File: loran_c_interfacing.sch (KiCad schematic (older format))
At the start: 16 parts, among them P401 SPI Bus A, P402 SPI Bus B, U401 74AC14, U402 74AC14

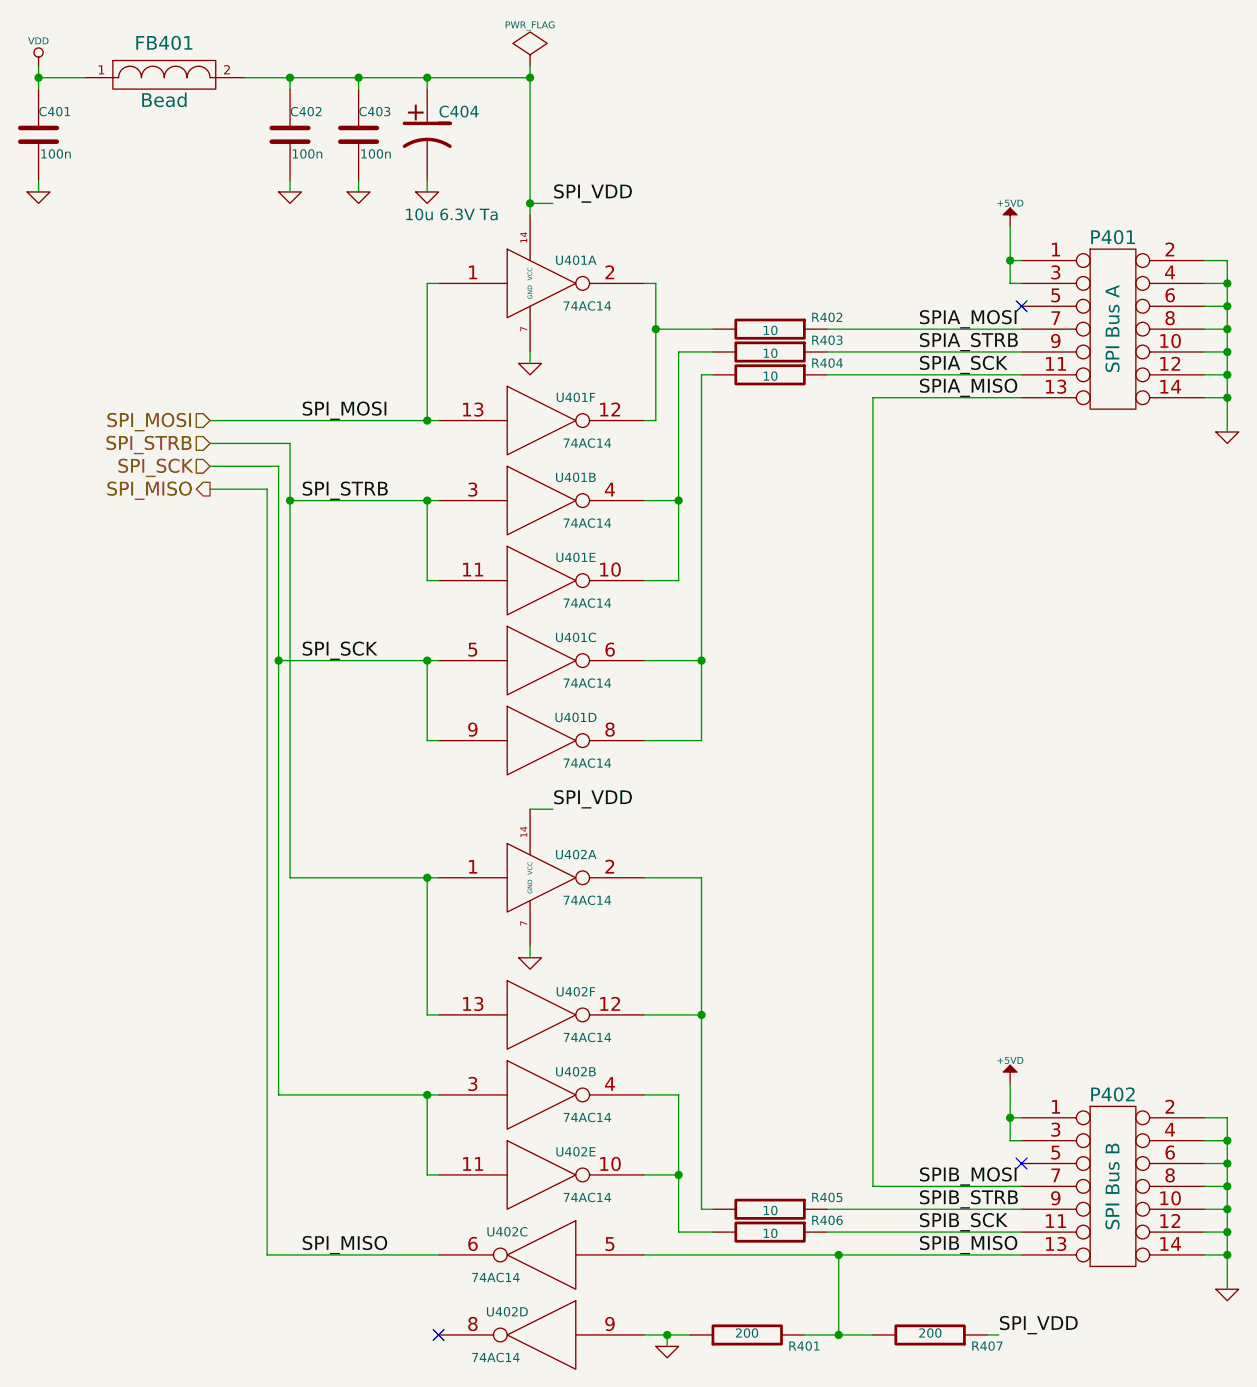
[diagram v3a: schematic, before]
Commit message: Update: minor schematic rework (due to PCB routing), PCB routing in early stage
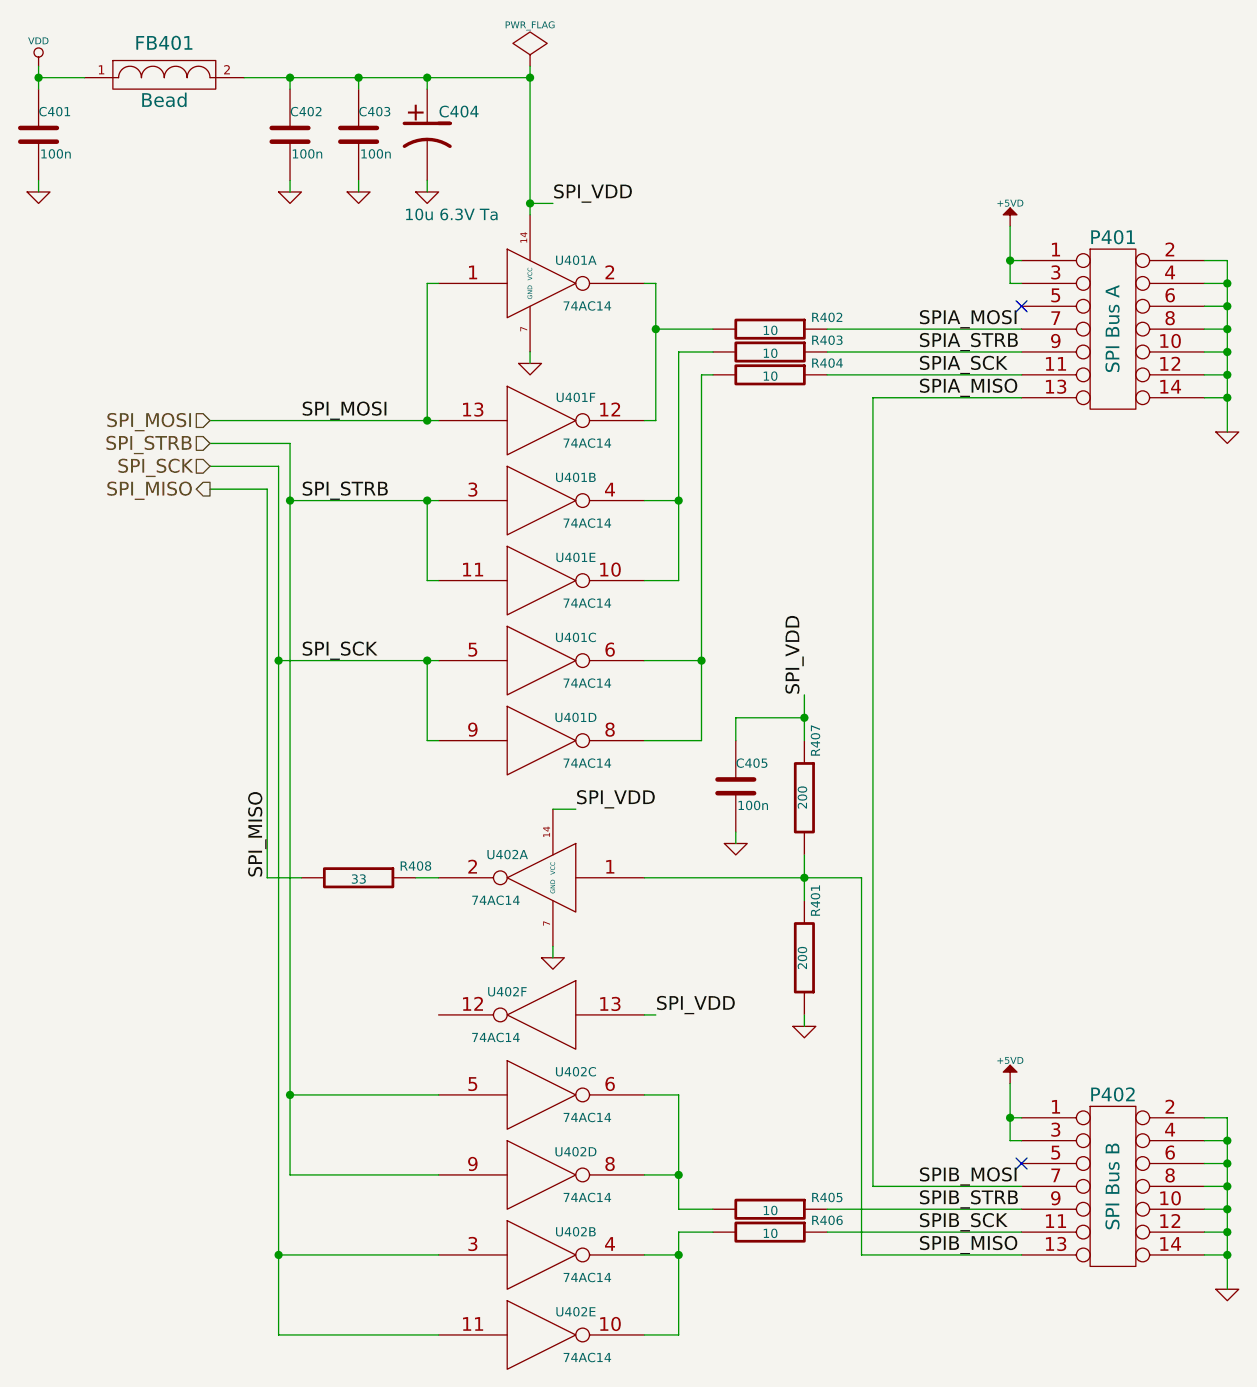
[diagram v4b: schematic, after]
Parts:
- added C405: 100n, w_smd_capacitors:c_1206, symbol C
- added R408: 33, w_smd_resistors:r_1206, symbol R
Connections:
- net GND: now also C405.2; no longer U402.9
- net SPIB_MISO: now also U402.1; no longer U402.5
- net SPI_MISO: now also R408.2; no longer U402.6
- net SPI_SCK: now also U402.11, U402.3; no longer U402.11, U402.3
- net SPI_STRB: now also U402.5, U402.9; no longer U402.1, U402.13
- net SPI_VDD: now also U402.13, C405.1
- new net: R408.1, U402.2
- new net: R405.2, U402.6, U402.8
- new net: R406.2, U402.10, U402.4
- now unconnected: U402.12
- no-connect marks 3 -> 2
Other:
- moved on the sheet: R401, R407
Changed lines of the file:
@@
 $EndComp
 $Comp
-L GND #PWR058
+L GND #PWR078
 U 1 1 52DAD917
 P 8600 2350
-F 0 "#PWR058" H 8600 2350 30  0001 C CNN
+F 0 "#PWR078" H 8600 2350 30  0001 C CNN
 F 1 "GND" H 8600 2280 30  0001 C CNN
 F 2 "" H 8600 2350 60  0000 C CNN
@@
 $EndComp
 $Comp
-L +5VD #PWR059
+L +5VD #PWR079
 U 1 1 52DAE845
 P 7650 1450
-F 0 "#PWR059" H 7650 1400 20  0001 C CNN
+F 0 "#PWR079" H 7650 1400 20  0001 C CNN
 F 1 "+5VD" H 7650 1550 30  0000 C CNN
 F 2 "" H 7650 1450 60  0000 C CNN
@@
 $EndComp
 $Comp
-L GND #PWR060
+L GND #PWR080
 U 1 1 52DAF90C
 P 8600 6100
-F 0 "#PWR060" H 8600 6100 30  0001 C CNN
+F 0 "#PWR080" H 8600 6100 30  0001 C CNN
 F 1 "GND" H 8600 6030 30  0001 C CNN
 F 2 "" H 8600 6100 60  0000 C CNN
@@
 $EndComp
 $Comp
-L +5VD #PWR061
+L +5VD #PWR081
 U 1 1 52DAF91B
 P 7650 5200
-F 0 "#PWR061" H 7650 5150 20  0001 C CNN
+F 0 "#PWR081" H 7650 5150 20  0001 C CNN
 F 1 "+5VD" H 7650 5300 30  0000 C CNN
 F 2 "" H 7650 5200 60  0000 C CNN
@@
 $EndComp
 $Comp
-L GND #PWR062
+L GND #PWR082
 U 1 1 52DD7CC9
 P 5550 2050
-F 0 "#PWR062" H 5550 2050 30  0001 C CNN
+F 0 "#PWR082" H 5550 2050 30  0001 C CNN
 F 1 "GND" H 5550 1980 30  0001 C CNN
 F 2 "" H 5550 2050 60  0000 C CNN
@@
 F 3 "" H 5600 4300 60  0000 C CNN
 	1    5600 4300
-	1    0    0    -1
-$EndComp
-$Comp
-L GND #PWR063
+	-1   0    0    -1
+$EndComp
+$Comp
+L GND #PWR083
 U 1 1 52DD892D
-P 5550 4650
-F 0 "#PWR063" H 5550 4650 30  0001 C CNN
-F 1 "GND" H 5550 4580 30  0001 C CNN
-F 2 "" H 5550 4650 60  0000 C CNN
-F 3 "" H 5550 4650 60  0000 C CNN
-	1    5550 4650
-	1    0    0    -1
-$EndComp
-Text Label 5650 4000 0    60   ~ 0
+P 5650 4650
+F 0 "#PWR083" H 5650 4650 30  0001 C CNN
+F 1 "GND" H 5650 4580 30  0001 C CNN
+F 2 "" H 5650 4650 60  0000 C CNN
+F 3 "" H 5650 4650 60  0000 C CNN
+	1    5650 4650
+	1    0    0    -1
+$EndComp
+Text Label 5750 4000 0    60   ~ 0
 SPI_VDD
 $Comp
@@
 F 3 "" H 5600 4900 60  0000 C CNN
 	6    5600 4900
-	1    0    0    -1
+	-1   0    0    -1
 $EndComp
 $Comp
 L 74HC14 U402
-U 2 1 52DD893F
+U 3 1 52DD893F
 P 5600 5250
 F 0 "U402" H 5750 5350 40  0000 C CNN
@@
 F 2 "w_smd_dil:so-16" H 5600 5250 60  0001 C CNN
 F 3 "" H 5600 5250 60  0000 C CNN
-	2    5600 5250
+	3    5600 5250
 	1    0    0    -1
 $EndComp
 $Comp
 L 74HC14 U402
-U 5 1 52DD8945
+U 4 1 52DD8945
 P 5600 5600
 F 0 "U402" H 5750 5700 40  0000 C CNN
@@
 F 2 "w_smd_dil:so-16" H 5600 5600 60  0001 C CNN
 F 3 "" H 5600 5600 60  0000 C CNN
-	5    5600 5600
+	4    5600 5600
 	1    0    0    -1
 $EndComp
 $Comp
 L 74HC14 U402
-U 3 1 52DD894B
+U 2 1 52DD894B
 P 5600 5950
 F 0 "U402" H 5750 6050 40  0000 C CNN
@@
 F 2 "w_smd_dil:so-16" H 5600 5950 60  0001 C CNN
 F 3 "" H 5600 5950 60  0000 C CNN
-	3    5600 5950
-	-1   0    0    -1
+	2    5600 5950
+	1    0    0    -1
 $EndComp
 $Comp
 L 74HC14 U402
-U 4 1 52DD8951
+U 5 1 52DD8951
 P 5600 6300
 F 0 "U402" H 5750 6400 40  0000 C CNN
@@
 F 2 "w_smd_dil:so-16" H 5600 6300 60  0001 C CNN
 F 3 "" H 5600 6300 60  0000 C CNN
-	4    5600 6300
-	-1   0    0    -1
-$EndComp
-$Comp
-L GND #PWR064
-U 1 1 52DD8B76
-P 6150 6350
-F 0 "#PWR064" H 6150 6350 30  0001 C CNN
-F 1 "GND" H 6150 6280 30  0001 C CNN
-F 2 "" H 6150 6350 60  0000 C CNN
-F 3 "" H 6150 6350 60  0000 C CNN
-	1    6150 6350
-	1    0    0    -1
-$EndComp
-NoConn ~ 5150 6300
+	5    5600 6300
+	1    0    0    -1
+$EndComp
 $Comp
 L R R405
@@
 L R R407
 U 1 1 52DDAE62
-P 7300 6300
-F 0 "R407" V 7250 6550 40  0000 C CNN
-F 1 "200" V 7307 6301 40  0000 C CNN
-F 2 "w_smd_resistors:r_1206" V 7230 6300 30  0001 C CNN
-F 3 "" H 7300 6300 30  0000 C CNN
-	1    7300 6300
-	0    1    -1   0
+P 6750 3950
+F 0 "R407" V 6700 4200 40  0000 C CNN
+F 1 "200" V 6757 3951 40  0000 C CNN
+F 2 "w_smd_resistors:r_1206" V 6680 3950 30  0001 C CNN
+F 3 "" H 6750 3950 30  0000 C CNN
+	1    6750 3950
+	-1   0    0    -1
 $EndComp
 $Comp
 L R R401
 U 1 1 52DDAF6A
-P 6500 6300
-F 0 "R401" V 6450 6050 40  0000 C CNN
-F 1 "200" V 6507 6301 40  0000 C CNN
-F 2 "w_smd_resistors:r_1206" V 6430 6300 30  0001 C CNN
-F 3 "" H 6500 6300 30  0000 C CNN
-	1    6500 6300
-	0    -1   -1   0
-$EndComp
-Text Label 7600 6300 0    60   ~ 0
+P 6750 4650
+F 0 "R401" V 6700 4400 40  0000 C CNN
+F 1 "200" V 6757 4651 40  0000 C CNN
+F 2 "w_smd_resistors:r_1206" V 6680 4650 30  0001 C CNN
+F 3 "" H 6750 4650 30  0000 C CNN
+	1    6750 4650
+	-1   0    0    1
+$EndComp
+Text Label 6750 3500 1    60   ~ 0
 SPI_VDD
 $Comp
@@
 $EndComp
 $Comp
-L VDD #PWR065
+L VDD #PWR084
 U 1 1 52DDD53B
 P 3400 750
-F 0 "#PWR065" H 3400 850 30  0001 C CNN
+F 0 "#PWR084" H 3400 850 30  0001 C CNN
 F 1 "VDD" H 3400 860 30  0000 C CNN
 F 2 "" H 3400 750 60  0000 C CNN
@@
 $EndComp
 $Comp
-L GND #PWR066
+L GND #PWR085
 U 1 1 52DDD665
 P 3400 1300
-F 0 "#PWR066" H 3400 1300 30  0001 C CNN
+F 0 "#PWR085" H 3400 1300 30  0001 C CNN
 F 1 "GND" H 3400 1230 30  0001 C CNN
 F 2 "" H 3400 1300 60  0000 C CNN
@@
 $EndComp
 $Comp
-L GND #PWR067
+L GND #PWR086
 U 1 1 52DDDBEB
 P 4500 1300
-F 0 "#PWR067" H 4500 1300 30  0001 C CNN
+F 0 "#PWR086" H 4500 1300 30  0001 C CNN
 F 1 "GND" H 4500 1230 30  0001 C CNN
 F 2 "" H 4500 1300 60  0000 C CNN
@@
 $EndComp
 $Comp
-L GND #PWR068
+L GND #PWR087
 U 1 1 52DDDCDD
 P 5100 1300
-F 0 "#PWR068" H 5100 1300 30  0001 C CNN
+F 0 "#PWR087" H 5100 1300 30  0001 C CNN
 F 1 "GND" H 5100 1230 30  0001 C CNN
 F 2 "" H 5100 1300 60  0000 C CNN
@@
 $EndComp
 $Comp
-L GND #PWR069
+L GND #PWR088
 U 1 1 52DDE27D
 P 4800 1300
-F 0 "#PWR069" H 4800 1300 30  0001 C CNN
+F 0 "#PWR088" H 4800 1300 30  0001 C CNN
 F 1 "GND" H 4800 1230 30  0001 C CNN
 F 2 "" H 4800 1300 60  0000 C CNN
@@
 Text Label 4550 3350 0    60   ~ 0
 SPI_SCK
-Text Label 4550 5950 0    60   ~ 0
+Text Label 4400 4300 1    60   ~ 0
 SPI_MISO
 NoConn ~ 7700 1800
@@
 	7050 5650 7700 5650
 Wire Wire Line
-	6200 5850 6350 5850
-Wire Wire Line
 	6850 5850 7700 5850
 Wire Wire Line
@@
 Connection ~ 7650 5350
 Wire Wire Line
-	6300 5750 6350 5750
-Wire Wire Line
 	6850 5750 7700 5750
 Wire Wire Line
@@
 Connection ~ 5550 1350
 Wire Wire Line
-	5550 4600 5550 4650
-Wire Wire Line
-	6050 6300 6250 6300
-Wire Wire Line
-	6150 6300 6150 6350
-Wire Wire Line
-	5550 4000 5650 4000
-Wire Wire Line
-	6050 4300 6300 4300
-Wire Wire Line
-	6300 4300 6300 5750
-Wire Wire Line
-	6300 4900 6050 4900
+	5650 4600 5650 4650
+Wire Wire Line
+	5650 4000 5750 4000
 Wire Wire Line
 	6050 5250 6200 5250
-Wire Wire Line
-	6200 5250 6200 5850
-Wire Wire Line
-	4500 4300 5150 4300
-Wire Wire Line
-	5100 4300 5100 4900
-Wire Wire Line
-	5100 4900 5150 4900
-Wire Wire Line
-	4450 5250 5150 5250
-Wire Wire Line
-	5100 5250 5100 5600
 Wire Wire Line
 	6050 1700 6100 1700
@@
 Wire Wire Line
 	6200 5600 6050 5600
-Wire Wire Line
-	5100 5600 5150 5600
 Connection ~ 6200 5600
-Connection ~ 6300 4900
-Connection ~ 6150 6300
-Wire Wire Line
-	6750 6300 7050 6300
-Wire Wire Line
-	7600 6300 7550 6300
-Connection ~ 6900 6300
-Wire Wire Line
-	6050 5950 7700 5950
-Wire Wire Line
-	6900 5950 6900 6300
-Connection ~ 6900 5950
-Wire Wire Line
-	4400 5950 5150 5950
 Wire Wire Line
 	3400 750  3400 850
@@
 Connection ~ 5100 2650
 Connection ~ 5100 3350
-Connection ~ 5100 4300
-Connection ~ 5100 5250
 Text HLabel 4150 2400 0    60   Input ~ 0
 SPI_STRB
@@
 	4150 2400 4500 2400
 Wire Wire Line
-	4500 2400 4500 4300
-Wire Wire Line
 	4150 2500 4450 2500
 Wire Wire Line
-	4450 2500 4450 5250
-Wire Wire Line
 	4150 2600 4400 2600
-Wire Wire Line
-	4400 2600 4400 5950
 Connection ~ 4500 2650
 Connection ~ 4450 3350
 $Comp
-L PWR_FLAG #FLG070
+L PWR_FLAG #FLG089
 U 1 1 52E83610
 P 5550 750
-F 0 "#FLG070" H 5550 845 30  0001 C CNN
+F 0 "#FLG089" H 5550 845 30  0001 C CNN
 F 1 "PWR_FLAG" H 5550 930 30  0000 C CNN
 F 2 "" H 5550 750 60  0000 C CNN
@@
 $EndComp
 Connection ~ 5550 800
+$Comp
+L R R408
+U 1 1 52E62630
+P 4800 4300
+F 0 "R408" V 4750 4550 40  0000 C CNN
+F 1 "33" V 4807 4301 40  0000 C CNN
+F 2 "w_smd_resistors:r_1206" V 4730 4300 30  0001 C CNN
+F 3 "" H 4800 4300 30  0000 C CNN
+	1    4800 4300
+	0    1    1    0
+$EndComp
+Text Label 6100 4900 0    60   ~ 0
+SPI_VDD
+Wire Wire Line
+	6100 4900 6050 4900
+Wire Wire Line
+	6050 5950 6200 5950
+Wire Wire Line
+	6200 6300 6050 6300
+Wire Wire Line
+	4400 2600 4400 4300
+Wire Wire Line
+	6200 5750 6350 5750
+Wire Wire Line
+	6200 5250 6200 5750
+Wire Wire Line
+	6350 5850 6200 5850
+Wire Wire Line
+	6200 5850 6200 6300
+Connection ~ 6200 5950
+Wire Wire Line
+	4500 2400 4500 5600
+Wire Wire Line
+	4500 5250 5150 5250
+Wire Wire Line
+	4500 5600 5150 5600
+Connection ~ 4500 5250
+Wire Wire Line
+	4450 2500 4450 6300
+Wire Wire Line
+	4450 5950 5150 5950
+Wire Wire Line
+	4450 6300 5150 6300
+Connection ~ 4450 5950
+Wire Wire Line
+	4400 4300 4550 4300
+Wire Wire Line
+	5050 4300 5150 4300
+Wire Wire Line
+	6050 4300 7000 4300
+Wire Wire Line
+	7000 4300 7000 5950
+Wire Wire Line
+	7000 5950 7700 5950
+$Comp
+L GND #PWR090
+U 1 1 52E6603F
+P 6750 4950
+F 0 "#PWR090" H 6750 4950 30  0001 C CNN
+F 1 "GND" H 6750 4880 30  0001 C CNN
+F 2 "" H 6750 4950 60  0000 C CNN
+F 3 "" H 6750 4950 60  0000 C CNN
+	1    6750 4950
+	1    0    0    -1
+$EndComp
+Wire Wire Line
+	6750 4900 6750 4950
+Wire Wire Line
+	6750 4200 6750 4400
+Connection ~ 6750 4300
+Wire Wire Line
+	6750 3500 6750 3700
+$Comp
+L C C405
+U 1 1 52E66600
+P 6450 3900
+F 0 "C405" H 6450 4000 40  0000 L CNN
+F 1 "100n" H 6456 3815 40  0000 L CNN
+F 2 "w_smd_capacitors:c_1206" H 6488 3750 30  0001 C CNN
+F 3 "" H 6450 3900 60  0000 C CNN
+	1    6450 3900
+	1    0    0    -1
+$EndComp
+$Comp
+L GND #PWR091
+U 1 1 52E6660B
+P 6450 4150
+F 0 "#PWR091" H 6450 4150 30  0001 C CNN
+F 1 "GND" H 6450 4080 30  0001 C CNN
+F 2 "" H 6450 4150 60  0000 C CNN
+F 3 "" H 6450 4150 60  0000 C CNN
+	1    6450 4150
+	1    0    0    -1
+$EndComp
+Connection ~ 6750 3600
+Wire Wire Line
+	6450 3700 6450 3600
+Wire Wire Line
+	6450 3600 6750 3600
+Wire Wire Line
+	6450 4100 6450 4150
 $EndSCHEMATC
